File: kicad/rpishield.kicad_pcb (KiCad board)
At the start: 2 copper layers, 65 x 56 mm, 23 parts

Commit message: SPI VCC, Jumper, MOSI track.
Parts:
- added JP1: Jumper, footprint:Custom_Pin_Header_Straight_1x02_Pitch2.54mm, F.Cu at (157.5, 77.5)
- moved R6 1.27 mm to (151.1, 73.7)
- moved R7 1.27 mm to (161.3, 73.7)
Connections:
- Conn2 pad 8: /RX -> Net-(Conn2-Pad8)
- Conn3 pad 17: Net-(Conn3-Pad17) -> /SPI_MOSI
- Conn3 pad 18: /SPI_MOSI -> Net-(Conn3-Pad18)
- R6 pad 1: /TX -> Net-(JP1-Pad2)
- R7 pad 1: /TX -> Net-(JP1-Pad2)
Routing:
- net /RX: track 56.0 -> 5.08 mm
- net Net-(JP1-Pad2): track 0.00 -> 6.35 mm
- net /TX: track 14.0 -> 8.89 mm
- net /SPI_MOSI: track 19.9 -> 17.3 mm
- net /VCC_LED: track 28.0 -> 25.9 mm
- net /VCC_ADC: track 69.6 -> 68.1 mm
- net /RX_RPI: track 18.4 -> 17.9 mm

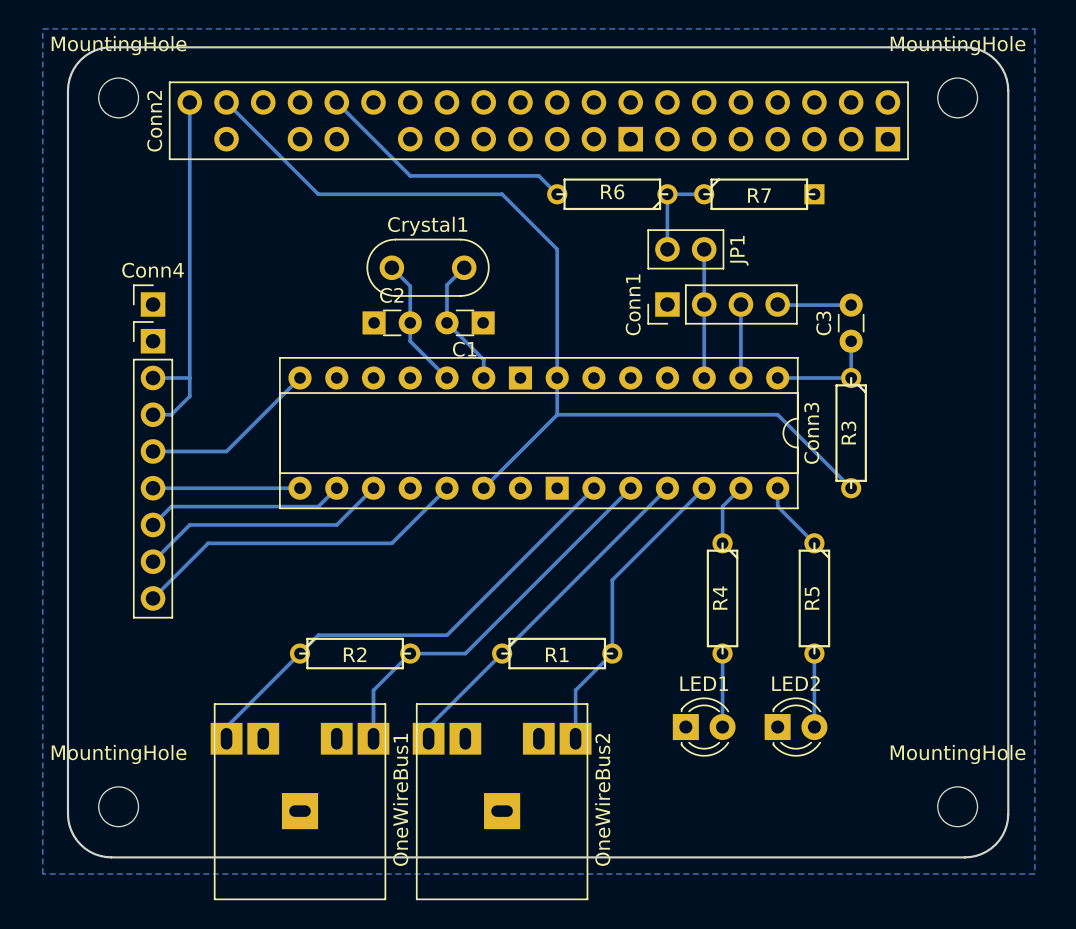
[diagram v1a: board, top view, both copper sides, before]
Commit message: 0.3mm track.
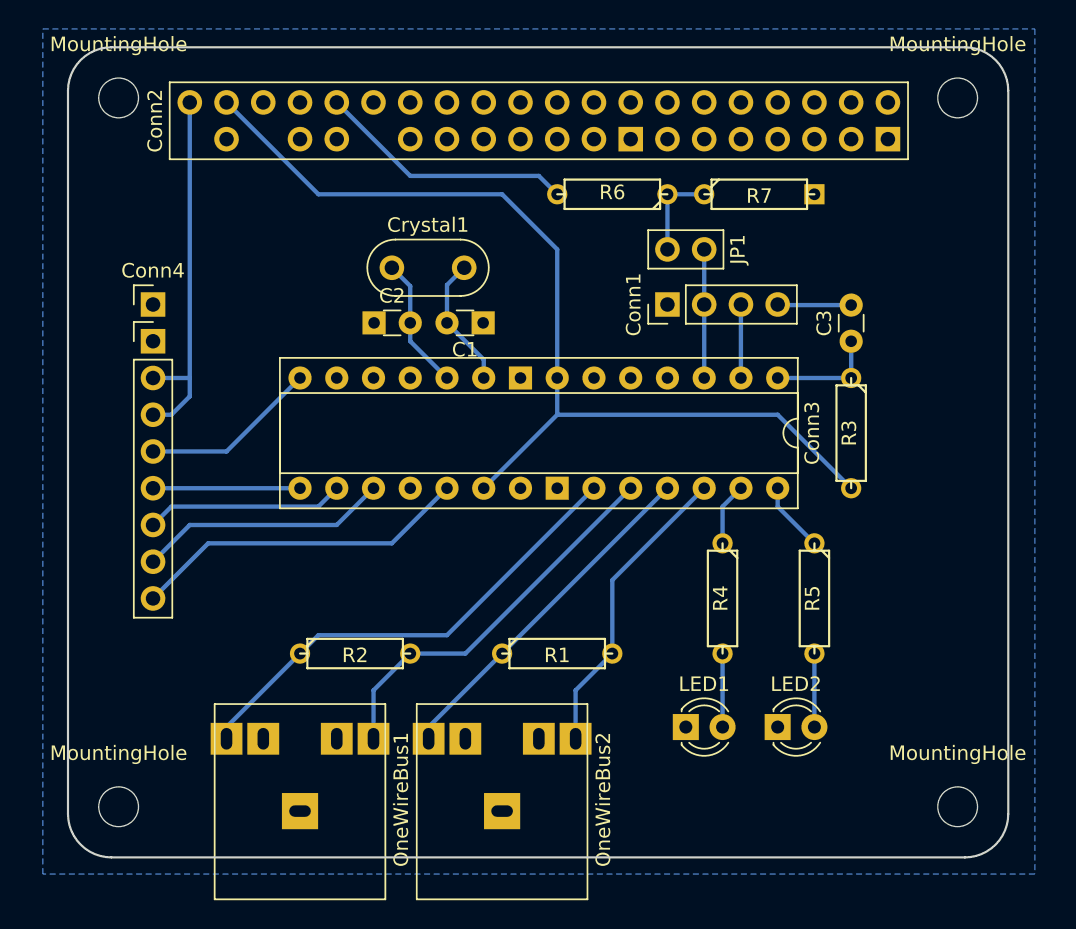
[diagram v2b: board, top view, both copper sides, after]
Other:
- net class Default: trace_width 0.254 -> 0.3
- rule trace_min: 0.254 -> 0.3

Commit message: R/C footprint pad + 0.625 mm.
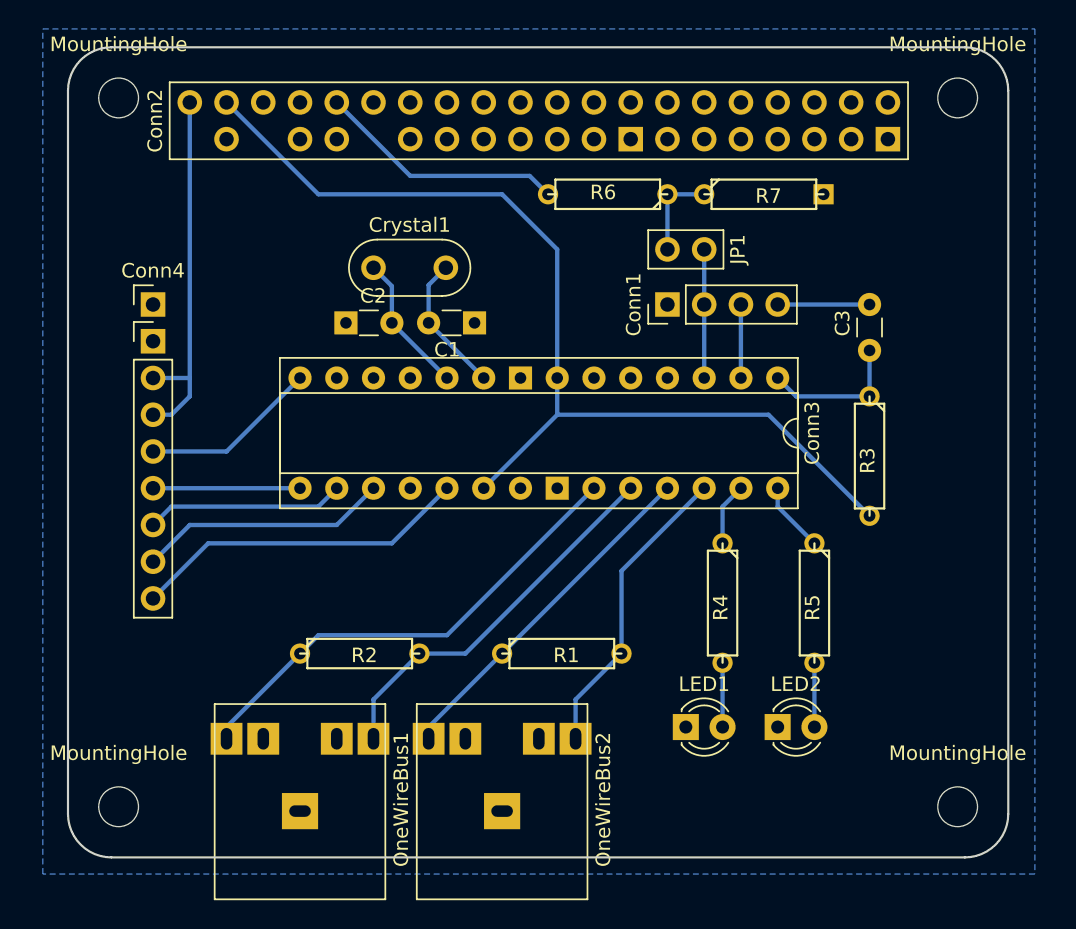
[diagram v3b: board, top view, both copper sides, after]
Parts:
- C1, C2: footprint footprint:Custom_Disc_D3.0mm_W1.6mm_P2.50mm -> footprint:Custom_Disc_D3.0mm_W1.6mm_P3.175mm
- C3: footprint Capacitors_THT:C_Disc_D3.0mm_W1.6mm_P2.50mm -> footprint:Custom_Disc_D3.0mm_W1.6mm_P3.175mm_normal
- R1, R2, R3, R4, R5, R6: footprint Discret:R3 -> footprint:Custom_R3_normal
- moved C2 1.94 mm to (132.7, 82.5)
- moved R3 1.80 mm to (168.9, 91.4)
- moved C3 1.42 mm to (168.9, 84.5)
- moved Crystal1 1.27 mm to (134.6, 78.7)
- moved C1 0.59 mm to (141.6, 82.5)
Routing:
- net /RST: track 7.62 -> 10.1 mm
- net /VCC_ADC: track 68.1 -> 70.2 mm
- net Net-(C3-Pad2): track 5.04 -> 6.35 mm
- net Net-(LED2-Pad2): track 5.08 -> 4.44 mm
- net Net-(LED1-Pad2): track 5.08 -> 4.44 mm
- net /RX_RPI: track 17.9 -> 17.2 mm
- net /XTAL1: track 9.17 -> 9.69 mm
- net /XTAL2: track 9.20 -> 9.72 mm

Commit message: Layout tune, 3D offsets.
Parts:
- moved C3 1.91 mm to (168.9, 82.5), turned to 180 degrees
- moved R6 1.27 mm to (151.1, 74.9)
- moved R7 1.27 mm to (161.3, 74.9)
- moved Conn1 1.27 mm to (154.9, 82.5)
- moved JP1 1.27 mm to (157.5, 78.7)
- moved R3 1.27 mm to (168.9, 90.2)
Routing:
- net Net-(C3-Pad2): track 6.35 -> 3.18 mm
- net /TX: track 8.89 -> 7.62 mm
- net /RX: track 5.08 -> 3.81 mm
- net /VCC_ADC: track 70.2 -> 69.6 mm
- net /RX_RPI: track 17.2 -> 17.8 mm
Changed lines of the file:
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@@
     (thickness 1.6)
     (drawings 8)
-    (tracks 65)
+    (tracks 64)
     (zones 0)
     (modules 24)
@@
   )
   (module Socket_Strips:Socket_Strip_Straight_1x04_Pitch2.54mm (layer F.Cu)
-    (at 154.94 81.28 90)
+    (at 154.94 82.55 90)
     (descr "Through hole straight socket strip, 1x04, 2.54mm pitch, single row")
     (tags "Through hole socket strip THT 1x04 2.54mm single row")
@@
   )
   (module footprint:Custom_Pin_Header_Straight_1x02_Pitch2.54mm (layer F.Cu)
-    (at 157.48 77.47 270)
+    (at 157.48 78.74 270)
     (descr "Through hole straight pin header, 1x02, 2.54mm pitch, single row")
     (tags "Through hole pin header THT 1x02 2.54mm single row")
@@
     (model Capacitors_THT.3dshapes/C_Disc_D3.0mm_W1.6mm_P2.50mm.wrl
       (at (xyz 0 0 0))
-      (scale (xyz 0.393701 0.393701 0.393701))
+      (scale (xyz 0.5 0.393701 0.5))
       (rotate (xyz 0 0 0))
     )
@@
     (model Capacitors_THT.3dshapes/C_Disc_D3.0mm_W1.6mm_P2.50mm.wrl
       (at (xyz 0 0 0))
-      (scale (xyz 0.393701 0.393701 0.393701))
+      (scale (xyz 0.5 0.393701 0.5))
       (rotate (xyz 0 0 0))
     )
   )
   (module footprint:Custom_Disc_D3.0mm_W1.6mm_P3.175mm_normal (layer F.Cu)
-    (at 168.91 84.455 90)
+    (at 168.91 82.55 180)
     (descr "C, Disc series, Radial, pin pitch=2.50mm, , diameter*width=3.0*1.6mm^2, Capacitor, http://www.vishay.com/docs/45233/krseries.pdf")
     (tags "C Disc series Radial pin pitch 2.50mm  diameter 3.0mm width 1.6mm Capacitor")
-    (fp_text reference C3 (at 1.885 -1.86 90) (layer F.SilkS)
-      (effects (font (size 1 1) (thickness 0.15)))
-    )
-    (fp_text value 100nF (at 1.25 1.86 90) (layer F.Fab)
+    (fp_text reference C3 (at 1.885 -1.86 180) (layer F.SilkS)
+      (effects (font (size 1 1) (thickness 0.15)))
+    )
+    (fp_text value 100nF (at 1.25 1.86 180) (layer F.Fab)
       (effects (font (size 1 1) (thickness 0.15)))
     )
@@
     (fp_line (start 4.205 1.15) (end 4.205 -1.15) (layer F.CrtYd) (width 0.05))
     (fp_line (start 4.205 -1.15) (end -1.03 -1.15) (layer F.CrtYd) (width 0.05))
-    (pad 1 thru_hole circle (at 0 0 90) (size 1.6 1.6) (drill 0.8) (layers *.Cu *.Mask)
+    (pad 1 thru_hole circle (at 0 0 180) (size 1.6 1.6) (drill 0.8) (layers *.Cu *.Mask)
       (net 4 /RST))
-    (pad 2 thru_hole circle (at 3.175 0 90) (size 1.6 1.6) (drill 0.8) (layers *.Cu *.Mask)
+    (pad 2 thru_hole circle (at 3.175 0 180) (size 1.6 1.6) (drill 0.8) (layers *.Cu *.Mask)
       (net 5 "Net-(C3-Pad2)"))
     (model Capacitors_THT.3dshapes/C_Disc_D3.0mm_W1.6mm_P2.50mm.wrl
       (at (xyz 0 0 0))
-      (scale (xyz 0.393701 0.393701 0.393701))
+      (scale (xyz 0.5 0.393701 0.5))
       (rotate (xyz 0 0 0))
     )
   )
   (module footprint:Custom_R3_normal (layer F.Cu)
-    (at 151.13 73.66 180)
+    (at 151.13 74.93 180)
     (descr "Resitance 3 pas")
     (tags R)
@@
       (net 17 /RX_RPI))
     (model Discret.3dshapes/R3.wrl
-      (at (xyz 0 0 0))
-      (scale (xyz 0.3 0.3 0.3))
+      (at (xyz 0.012 0 0))
+      (scale (xyz 0.325 0.3 0.3))
       (rotate (xyz 0 0 0))
     )
   )
   (module footprint:Custom_R3 (layer F.Cu)
-    (at 161.29 73.66)
+    (at 161.29 74.93)
     (descr "Resitance 3 pas")
     (tags R)
@@
       (net 1 GND))
     (model Discret.3dshapes/R3.wrl
-      (at (xyz 0 0 0))
-      (scale (xyz 0.3 0.3 0.3))
+      (at (xyz 0.012 0 0))
+      (scale (xyz 0.325 0.3 0.3))
       (rotate (xyz 0 0 0))
     )
@@
     (model Discret.3dshapes/R3.wrl
       (at (xyz 0 0 0))
-      (scale (xyz 0.3 0.3 0.3))
+      (scale (xyz 0.325 0.3 0.3))
       (rotate (xyz 0 0 0))
     )
@@
     (model Discret.3dshapes/R3.wrl
       (at (xyz 0 0 0))
-      (scale (xyz 0.3 0.3 0.3))
+      (scale (xyz 0.325 0.3 0.3))
       (rotate (xyz 0 0 0))
     )
@@
       (net 56 /BUS2_DQ))
     (model Discret.3dshapes/R3.wrl
-      (at (xyz 0 0 0))
-      (scale (xyz 0.3 0.3 0.3))
+      (at (xyz 0.012 0 0))
+      (scale (xyz 0.325 0.3 0.3))
       (rotate (xyz 0 0 0))
     )
@@
       (net 54 /BUS1_DQ))
     (model Discret.3dshapes/R3.wrl
-      (at (xyz 0 0 0))
-      (scale (xyz 0.3 0.3 0.3))
+      (at (xyz 0.012 0 0))
+      (scale (xyz 0.325 0.3 0.3))
       (rotate (xyz 0 0 0))
     )
   )
   (module footprint:Custom_R3_normal (layer F.Cu)
-    (at 168.91 91.44 270)
+    (at 168.91 90.17 270)
     (descr "Resitance 3 pas")
     (tags R)
@@
       (net 52 /VCC_ADC))
     (model Discret.3dshapes/R3.wrl
-      (at (xyz 0 0 0))
-      (scale (xyz 0.3 0.3 0.3))
+      (at (xyz 0.012 0 0))
+      (scale (xyz 0.325 0.3 0.3))
       (rotate (xyz 0 0 0))
     )
@@
   (segment (start 135.89 80.01) (end 134.62 78.74) (width 0.3) (layer B.Cu) (net 3))
   (segment (start 139.7 86.36) (end 135.89 82.55) (width 0.3) (layer B.Cu) (net 3))
-  (segment (start 168.91 87.63) (end 163.83 87.63) (width 0.3) (layer B.Cu) (net 4))
-  (segment (start 163.83 87.63) (end 162.56 86.36) (width 0.3) (layer B.Cu) (net 4))
-  (segment (start 168.91 84.455) (end 168.91 87.63) (width 0.3) (layer B.Cu) (net 4))
-  (segment (start 162.56 81.28) (end 168.91 81.28) (width 0.3) (layer B.Cu) (net 5))
-  (segment (start 157.48 81.28) (end 157.48 77.47) (width 0.3) (layer B.Cu) (net 6))
-  (segment (start 157.48 86.36) (end 157.48 81.28) (width 0.3) (layer B.Cu) (net 6))
-  (segment (start 160.02 81.28) (end 160.02 86.36) (width 0.3) (layer B.Cu) (net 7))
+  (segment (start 168.91 86.36) (end 168.91 82.55) (width 0.3) (layer B.Cu) (net 4))
+  (segment (start 162.56 86.36) (end 168.91 86.36) (width 0.3) (layer B.Cu) (net 4))
+  (segment (start 165.735 82.55) (end 162.56 82.55) (width 0.3) (layer B.Cu) (net 5))
+  (segment (start 157.48 86.36) (end 157.48 82.55) (width 0.3) (layer B.Cu) (net 6))
+  (segment (start 157.48 82.55) (end 157.48 78.74) (width 0.3) (layer B.Cu) (net 6))
+  (segment (start 160.02 86.36) (end 160.02 82.55) (width 0.3) (layer B.Cu) (net 7))
   (segment (start 158.75 106.045) (end 158.75 110.49) (width 0.3) (layer B.Cu) (net 15))
   (segment (start 165.1 106.045) (end 165.1 110.49) (width 0.3) (layer B.Cu) (net 16))
-  (segment (start 137.16 72.39) (end 145.415 72.39) (width 0.3) (layer B.Cu) (net 17))
-  (segment (start 145.415 72.39) (end 146.685 73.66) (width 0.3) (layer B.Cu) (net 17))
+  (segment (start 137.16 72.39) (end 144.145 72.39) (width 0.3) (layer B.Cu) (net 17))
+  (segment (start 144.145 72.39) (end 146.685 74.93) (width 0.3) (layer B.Cu) (net 17))
   (segment (start 132.08 67.31) (end 137.16 72.39) (width 0.3) (layer B.Cu) (net 17))
   (segment (start 121.92 87.63) (end 121.92 86.36) (width 0.3) (layer B.Cu) (net 46))
@@
   (segment (start 123.19 97.79) (end 135.89 97.79) (width 0.3) (layer B.Cu) (net 50))
   (segment (start 129.54 93.98) (end 119.38 93.98) (width 0.3) (layer B.Cu) (net 51))
-  (segment (start 147.32 88.9) (end 161.925 88.9) (width 0.3) (layer B.Cu) (net 52))
-  (segment (start 161.925 88.9) (end 168.91 95.885) (width 0.3) (layer B.Cu) (net 52))
+  (segment (start 147.32 88.9) (end 163.195 88.9) (width 0.3) (layer B.Cu) (net 52))
+  (segment (start 163.195 88.9) (end 168.91 94.615) (width 0.3) (layer B.Cu) (net 52))
   (segment (start 124.46 67.31) (end 130.81 73.66) (width 0.3) (layer B.Cu) (net 52))
   (segment (start 130.81 73.66) (end 143.51 73.66) (width 0.3) (layer B.Cu) (net 52))
@@
   (segment (start 162.56 93.98) (end 162.56 95.25) (width 0.3) (layer B.Cu) (net 58))
   (segment (start 162.56 95.25) (end 165.1 97.79) (width 0.3) (layer B.Cu) (net 58))
-  (segment (start 154.94 73.66) (end 157.48 73.66) (width 0.3) (layer B.Cu) (net 65))
-  (segment (start 154.94 77.47) (end 154.94 73.66) (width 0.3) (layer B.Cu) (net 65))
+  (segment (start 154.94 78.74) (end 154.94 74.93) (width 0.3) (layer B.Cu) (net 65))
+  (segment (start 154.94 74.93) (end 157.48 74.93) (width 0.3) (layer B.Cu) (net 65))
   (zone (net 1) (net_name GND) (layer B.Cu) (hatch edge 0.508)
     (connect_pads (clearance 0.508))
